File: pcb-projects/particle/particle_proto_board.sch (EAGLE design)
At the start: 20 parts, among them IC1 ATTINY20-SOIC-14S1, IC2 DMC2400UV-SOT563, IC3 DMC2400UV-SOT563, X1 332-04

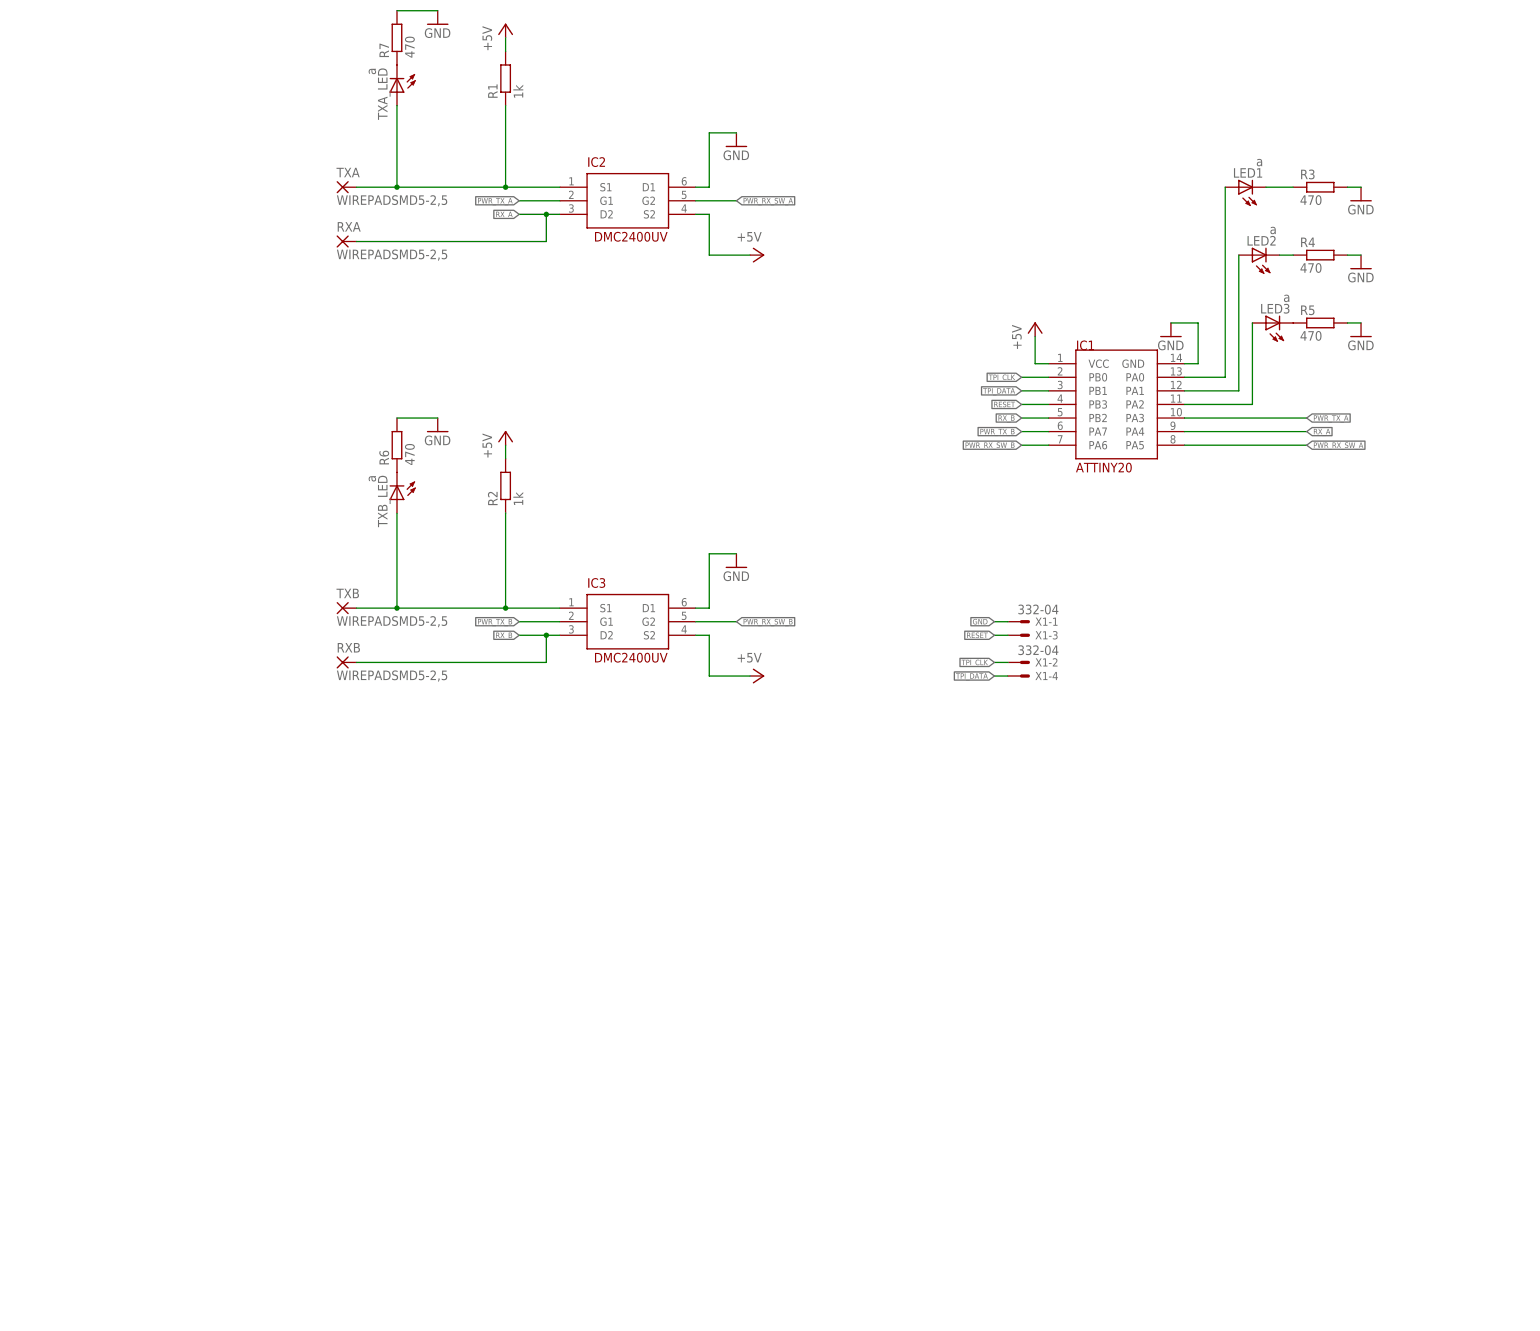
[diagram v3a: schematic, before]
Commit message: added test pins
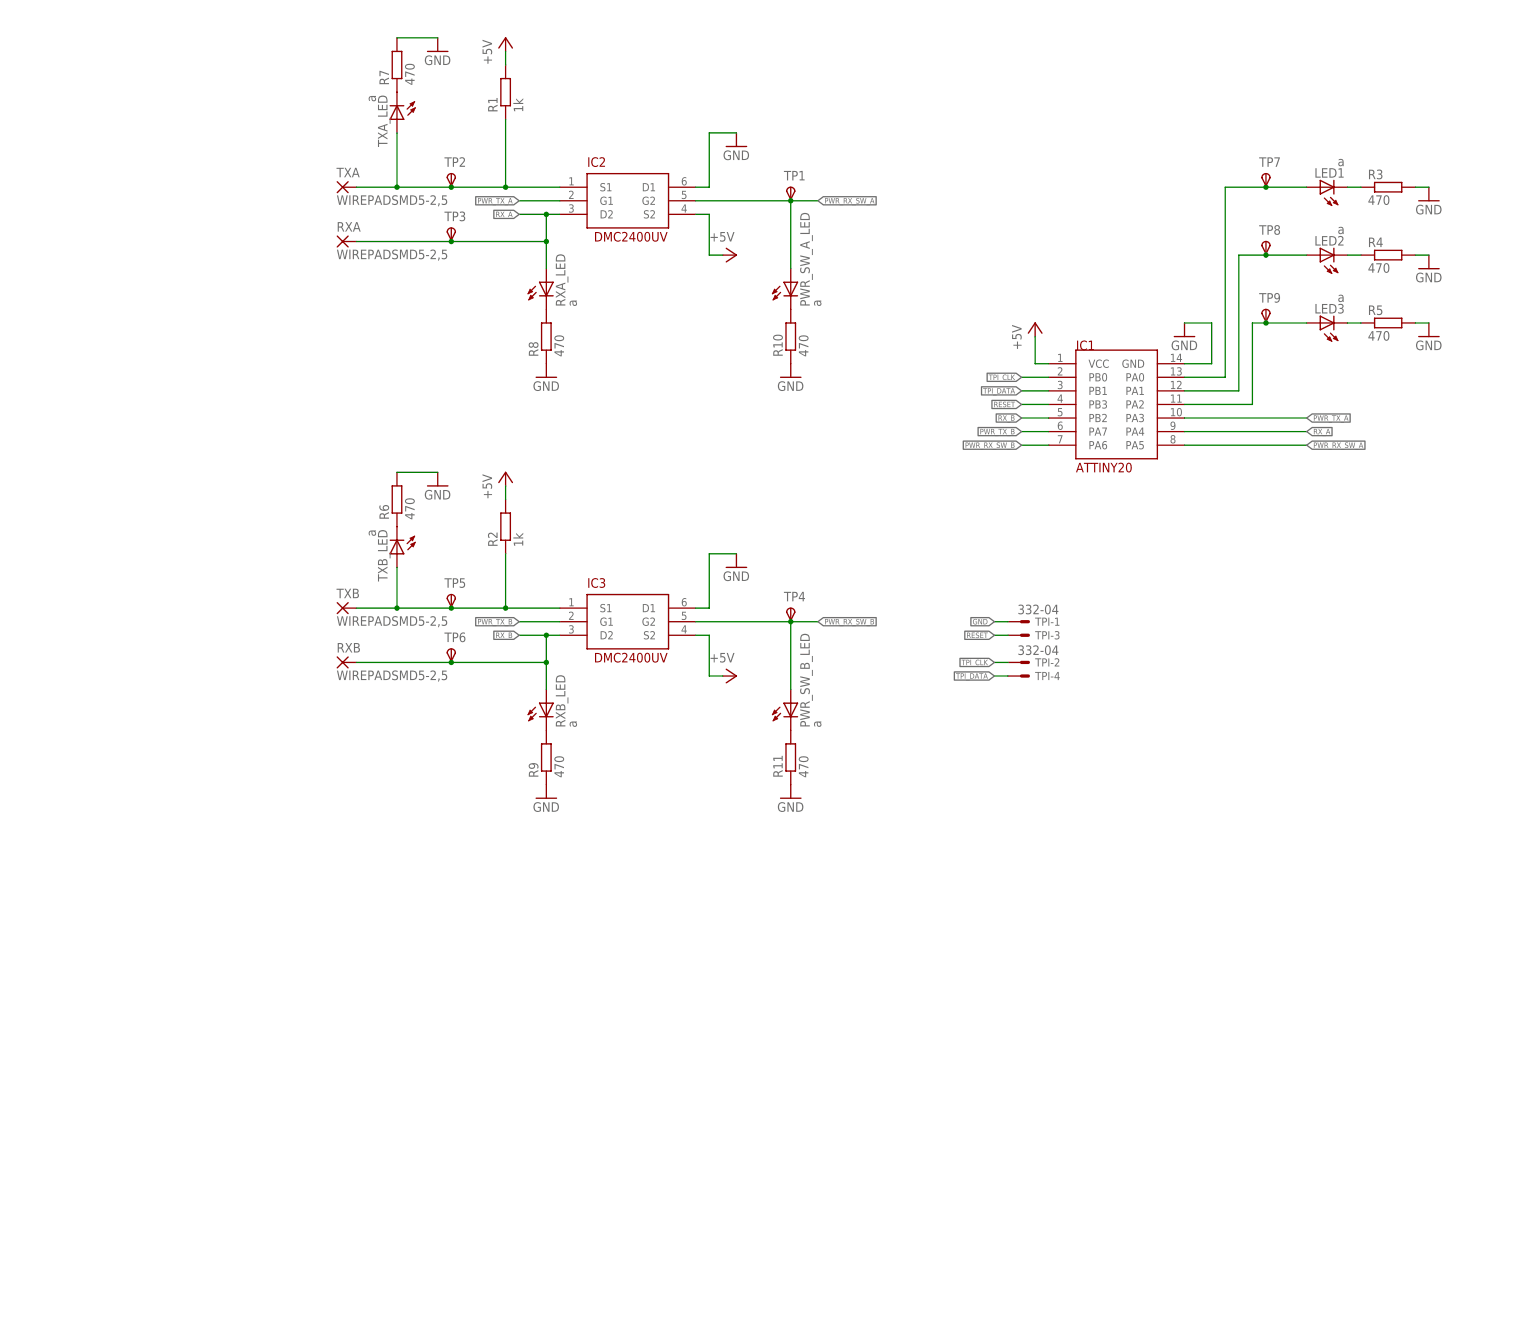
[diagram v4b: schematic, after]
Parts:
- added PWR_SW_A_LED, PWR_SW_B_LED, RXA_LED, RXB_LED: a, led:LEDKA-3528ASYC
- added R10, R11, R8, R9: 470, rcl:R-EU_R1206
- added TP1, TP2, TP3, TP4, TP5, TP6, TP7, TP8, TP9: TPSPAD1-13, testpad:TPSPAD1-13
- renumbered X1 to TPI
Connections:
- new net N$11: R8.2, RXA_LED.C
- new net N$12: R9.2, RXB_LED.C
- new net N$13: PWR_SW_A_LED.C, R10.2
- new net N$14: PWR_SW_B_LED.C, R11.2
- net GND: now also R10.1, R11.1, R8.1, R9.1
- net N$1: now also TP7.PP
- net N$2: now also TP9.PP
- net N$3: now also TP8.PP
- net PWR_RX_SW_A: now also PWR_SW_A_LED.A, TP1.PP
- net PWR_RX_SW_B: now also PWR_SW_B_LED.A, TP4.PP
- net PWR_TX_A_A_A: now also TP2.PP
- net RX_A: now also RXA_LED.A, TP3.PP
- net RX_B: now also RXB_LED.A, TP6.PP
- net TXB: now also TP5.PP
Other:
- moved on the sheet: LED1, LED2, LED3, R1, R2, R3, R4, R5, R6, R7, TXA_LED, TXB_LED

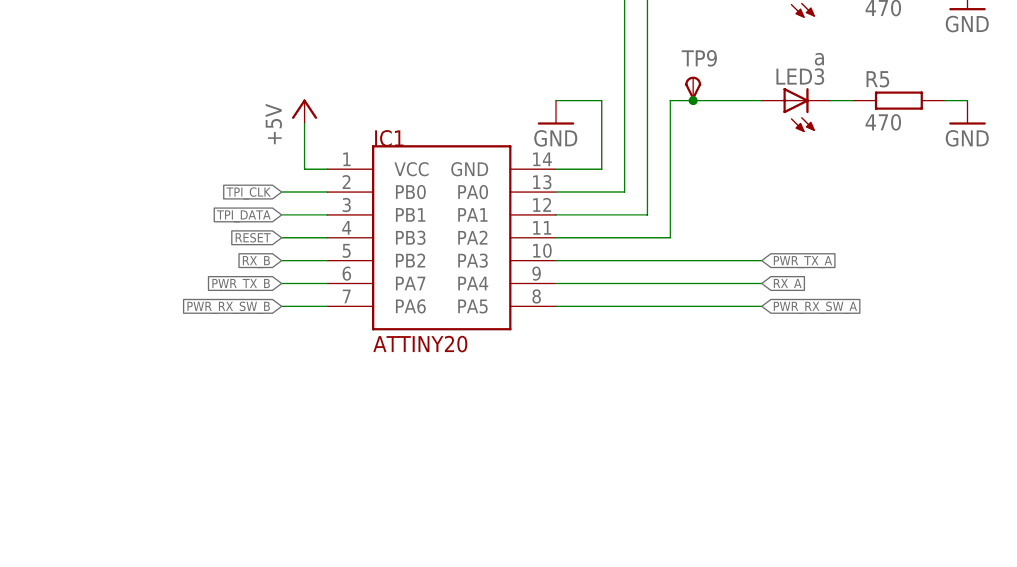
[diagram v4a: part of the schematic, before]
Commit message: routed bard
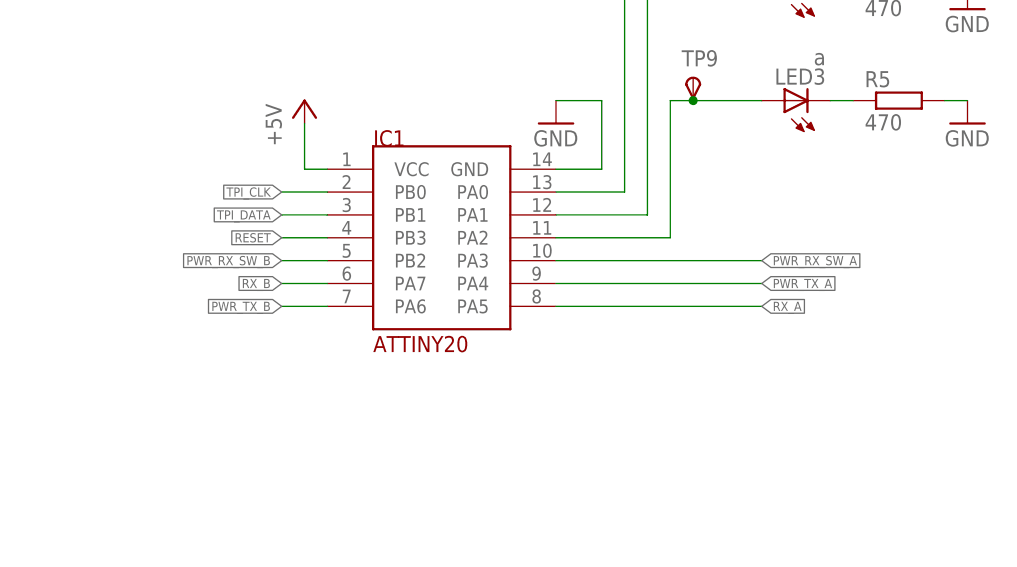
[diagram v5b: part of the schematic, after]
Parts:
- LED1, LED2, LED3, PWR_SW_A_LED, PWR_SW_B_LED, RXA_LED, RXB_LED, TXA_LED, TXB_LED: device led:LEDKA-3528ASYC -> led:LEDSML1206
- R1, R10, R11, R2, R3, R4, R5, R6, R7, R8, R9: device rcl:R-EU_R1206 -> rcl:R-EU_R1210
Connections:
- net PWR_RX_SW_A: now also IC1.PA3; no longer IC1.PA5
- net PWR_RX_SW_B: now also IC1.PB2; no longer IC1.PA6
- net PWR_TX_A: now also IC1.PA4; no longer IC1.PA3
- net PWR_TX_B: now also IC1.PA6; no longer IC1.PA7
- net RX_A: now also IC1.PA5; no longer IC1.PA4
- net RX_B: now also IC1.PA7; no longer IC1.PB2
